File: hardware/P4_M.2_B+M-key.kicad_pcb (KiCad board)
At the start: 4 copper layers, 22 x 42 mm, 87 parts, among them IC1 XT25F128FWOIGT-W, IC2 TPS563202DRLR, IC4 TPS563202DRLR, J2 USB_C_Receptacle_USB2.0_16P, Q2 MMDT2222A, U2 ESP32-P4NRW16, U3 EMMC04G-W627-M06U, U5 CH340K, Y1 32KHz, Y2 40MHz

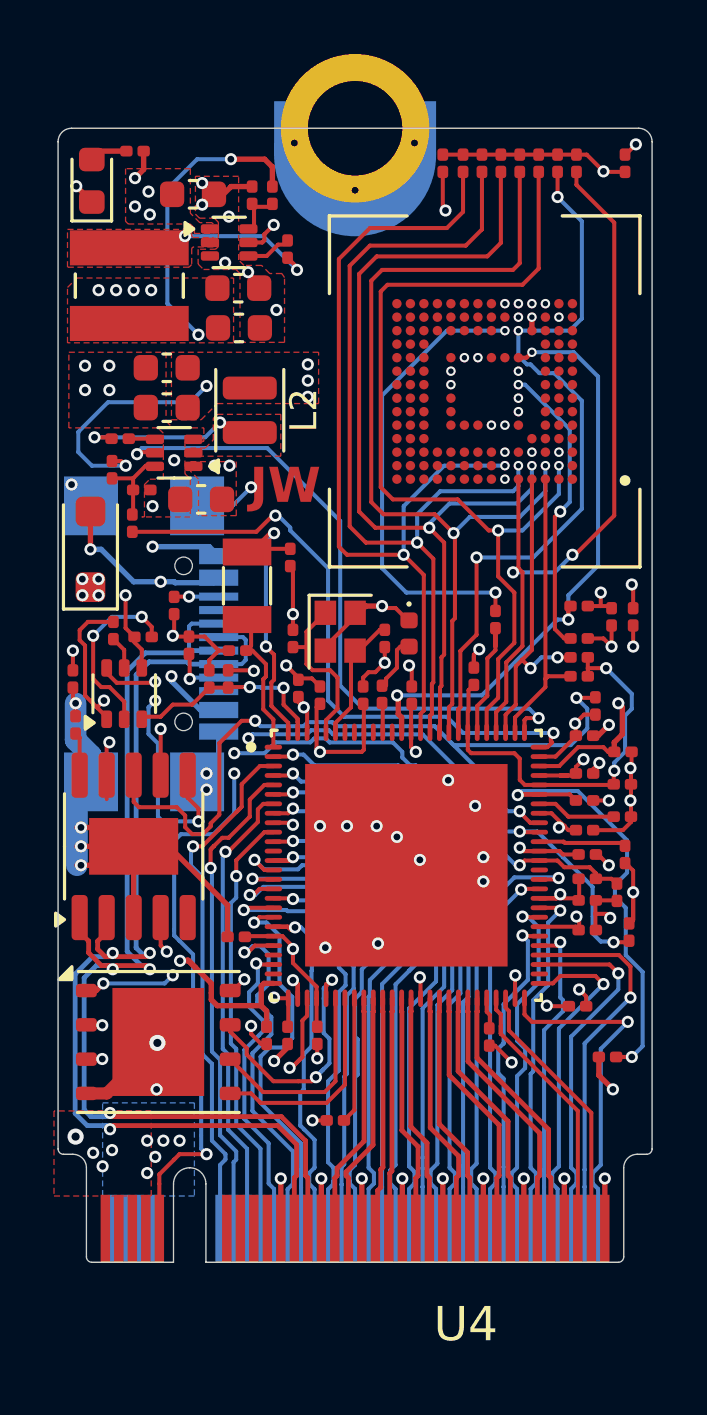
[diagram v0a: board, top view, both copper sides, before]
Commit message: Updated module, now with uSD
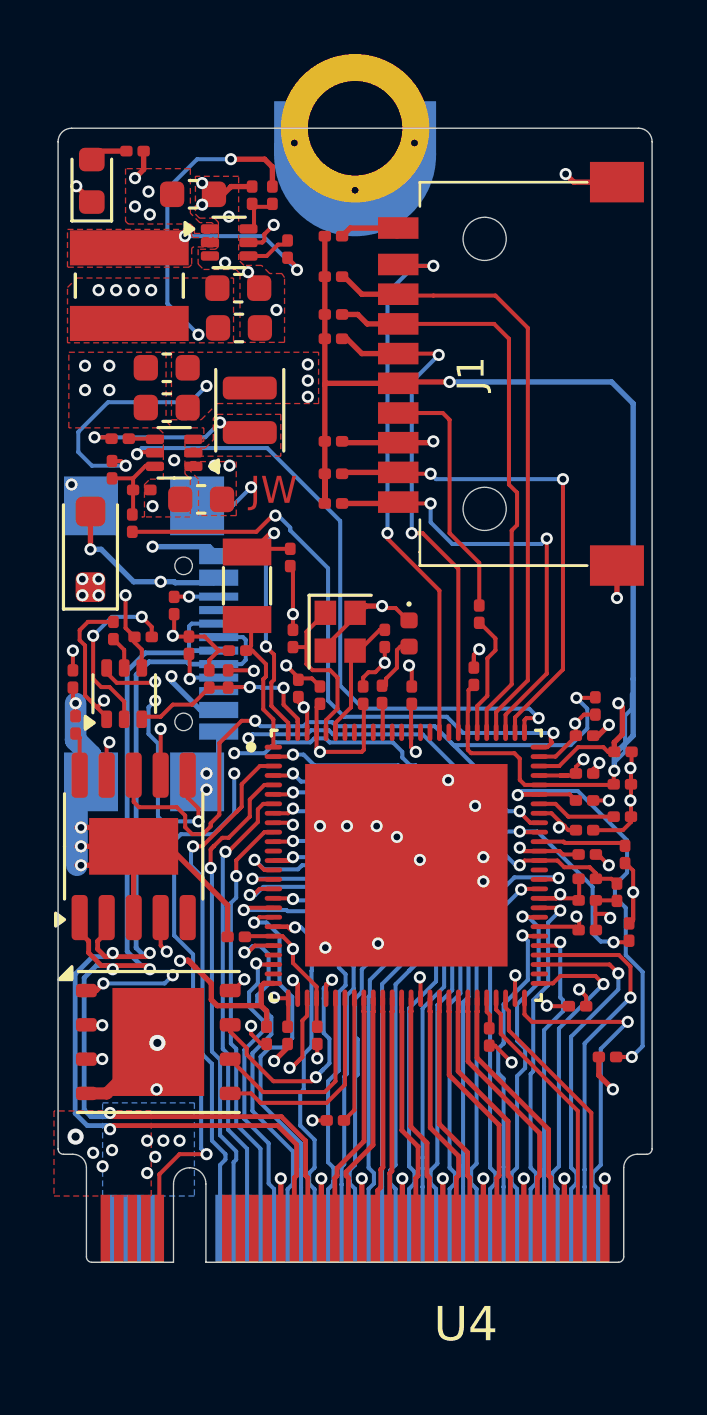
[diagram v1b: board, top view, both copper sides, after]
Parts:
- removed C30: 4.7uF, Capacitor_SMD:C_0201_0603Metric
- removed C31, C35, C36: 100nF, Capacitor_SMD:C_0201_0603Metric
- removed R15, R16, R17: 51K, Resistor_SMD:R_0201_0603Metric
- removed R20: 10k, Resistor_SMD:R_0201_0603Metric
- removed R21: 100K, Resistor_SMD:R_0201_0603Metric
- removed U3: EMMC04G-W627-M06U, P4_M.2_B+M-key:BGA153N50P14X14_1300X1150X100N
- added C38: 100nF, Capacitor_SMD:C_0201_0603Metric, F.Cu at (147.7, 95.6)
- added J1: Micro_SD_Card_Det2, WHY:uSD_CARD, F.Cu at (153.3, 93.1)
- moved R10 11.8 mm to (147.7, 96.8), turned to 0 degrees
- moved R11 10.7 mm to (147.7, 97.9), turned to 0 degrees
- moved R19 10.5 mm to (147.7, 91.8), turned to 0 degrees
- moved R12 9.93 mm to (147.7, 89.5), turned to 0 degrees
- moved R13 9.44 mm to (147.7, 90.9), turned to 0 degrees
- moved R14 7.41 mm to (147.7, 88.0), turned to 0 degrees
- moved R18 0.63 mm to (153.1, 102.0)
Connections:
- R14 pad 2: /SD_DATA4 -> Net-(J1-DET_A)
- U2 pad 49: /USB2HS_D+ -> /USB2HS_D-
- U2 pad 50: /USB2HS_D- -> /USB2HS_D+
- U2 pad 87: /SD_DATA4 -> unconnected-(U2A-GPIO45-Pad87)
- U2 pad 88: /SD_DATA5 -> /SD_DET
- U2 pad 89: /SD_DATA6 -> unconnected-(U2A-GPIO47-Pad89)
- U2 pad 90: /SD_DATA7 -> unconnected-(U2A-GPIO48-Pad90)
- U4 pad 3: /USB2HS_D- -> /USB2HS_D+
- U4 pad 5: /USB2HS_D+ -> /USB2HS_D-
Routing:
- net /SD_DATA4: track 33.4 -> 0.00 mm, vias 2 -> 0
- net /SD_DATA6: track 33.3 -> 0.00 mm, vias 2 -> 0
- net /SD_DATA5: track 33.2 -> 0.00 mm, vias 2 -> 0
- net /SD_DATA7: track 33.1 -> 0.00 mm, vias 2 -> 0
- net /REST_N: track 22.3 -> 0.00 mm, vias 3 -> 0
- net /SD_DET: track 0.00 -> 20.5 mm, vias 0 -> 2
- net /SD_DATA3: track 34.1 -> 21.7 mm, vias 2 -> 0
- net Net-(U3A-DS): track 10.9 -> 0.00 mm, vias 2 -> 0
- net /SD_CMD: track 28.7 -> 19.2 mm, vias 3 -> 2
- net Net-(J1-CLK): track 17.2 -> 9.34 mm, vias 2 -> 0
- net /SD_DATA0: track 10.8 -> 18.4 mm, vias 0 -> 2
- net /SD_DATA2: track 28.0 -> 23.1 mm, vias 2 -> 0
- net /SD_DATA1: track 11.9 -> 16.5 mm
- net Net-(J1-DET_A): track 0.00 -> 2.27 mm
- net GND: track 89.0 -> 90.2 mm, vias 82 -> 70
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
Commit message: Fixed mistakes from prototype 1
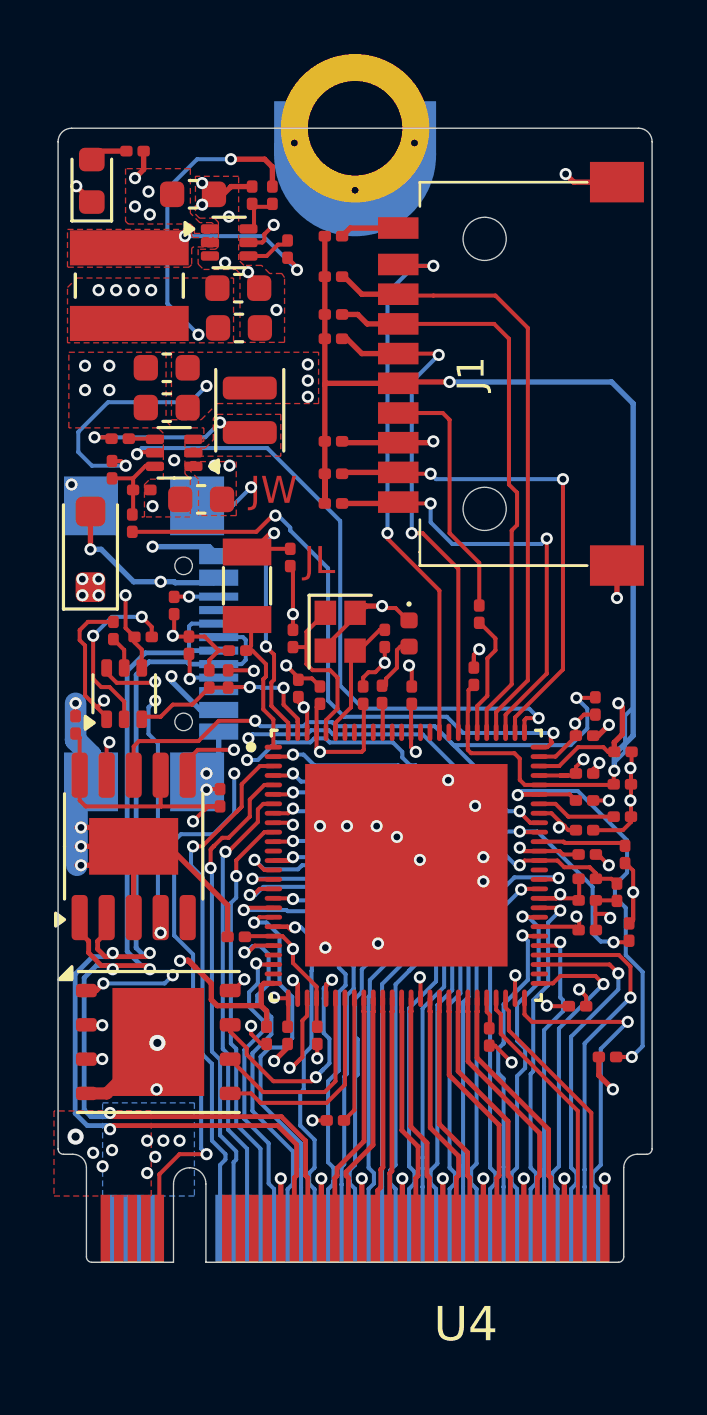
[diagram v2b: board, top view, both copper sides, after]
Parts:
- moved C50 7.00 mm to (143.5, 108.8), turned to -90 degrees
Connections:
- C2 pad 2: Net-(U5-V3) -> /3.3V
- C50 pad 2: /USB5V -> /3.3V
- Q2 pad 1: /RTS -> /DTR
- Q2 pad 4: /DTR -> /RTS
- R30 pad 1: /DTR -> /RTS
- R31 pad 1: /RTS -> /DTR
- U5 pad 10: Net-(U5-V3) -> /3.3V
- U5 pad 7: /USB5V -> /3.3V
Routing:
- net /3.3V: track 47.5 -> 57.7 mm, vias 23 -> 24
- net /GPIO38: track 29.4 -> 25.8 mm
- net /DTR: track 19.6 -> 16.3 mm, vias 2 -> 3
- net /USB5V: track 9.52 -> 6.21 mm, vias 17 -> 15
- net Net-(U5-V3): track 1.60 -> 0.00 mm
- net /RTS: track 15.4 -> 16.2 mm, vias 3 -> 2
- net /V/SDMMC: track 49.3 -> 48.8 mm
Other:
- board text added: "JL"
